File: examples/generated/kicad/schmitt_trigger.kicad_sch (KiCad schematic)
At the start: 6 parts

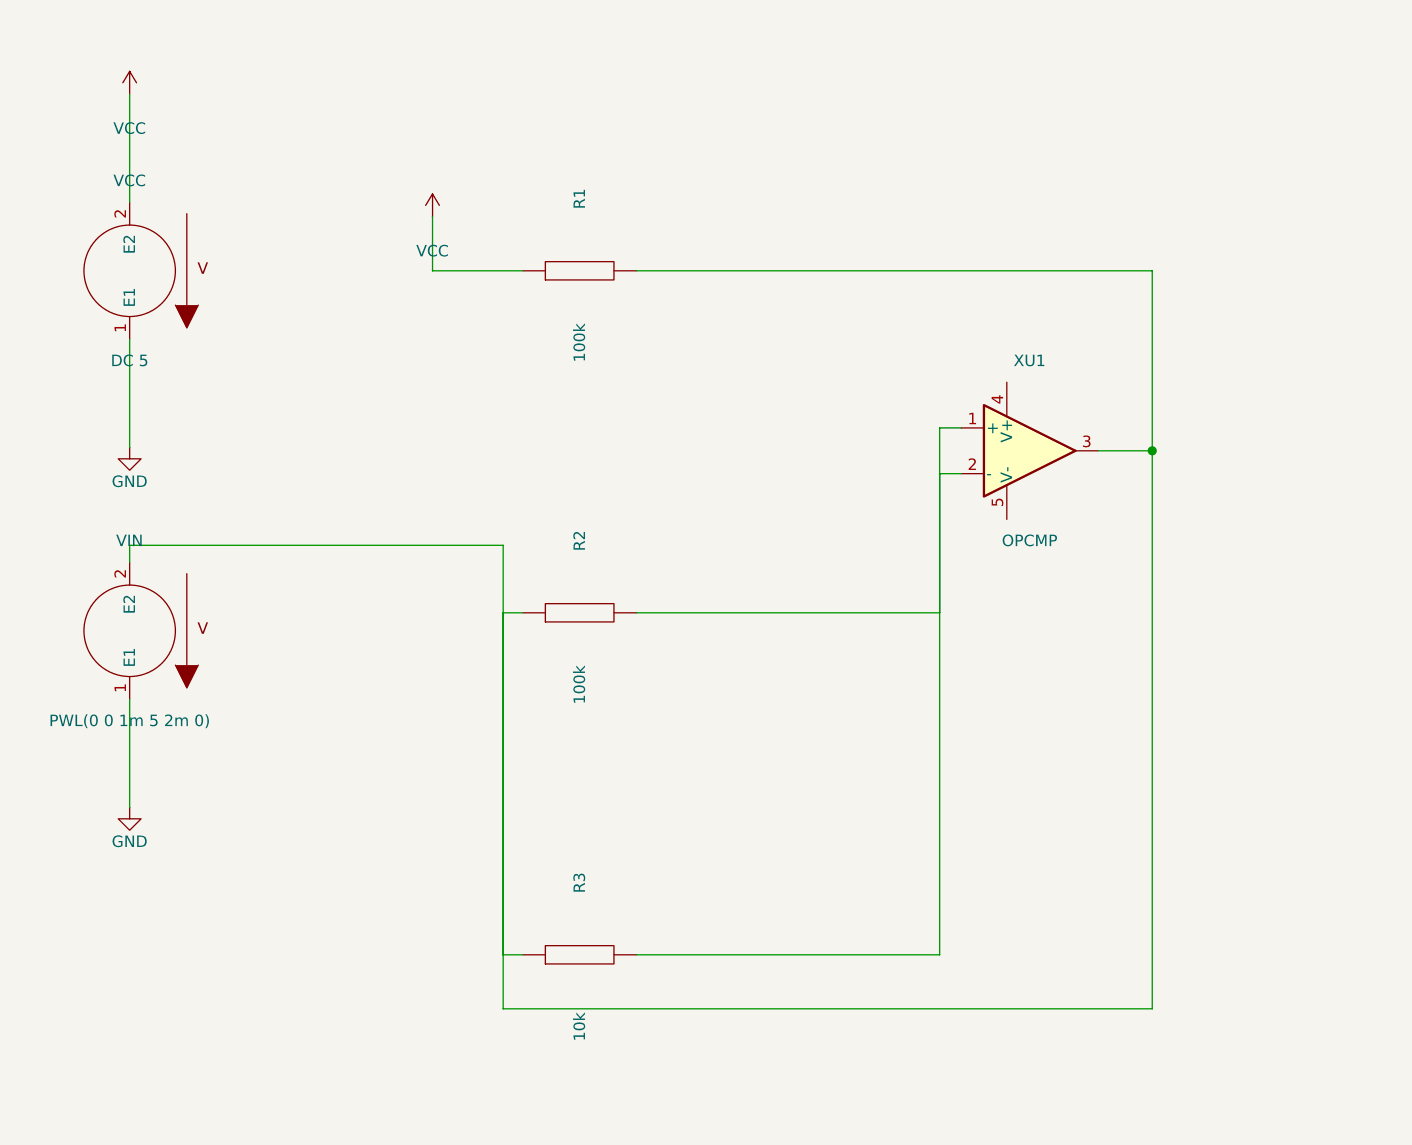
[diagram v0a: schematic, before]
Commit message: Ensure connectivity matches, as measured by opamp connectivity.
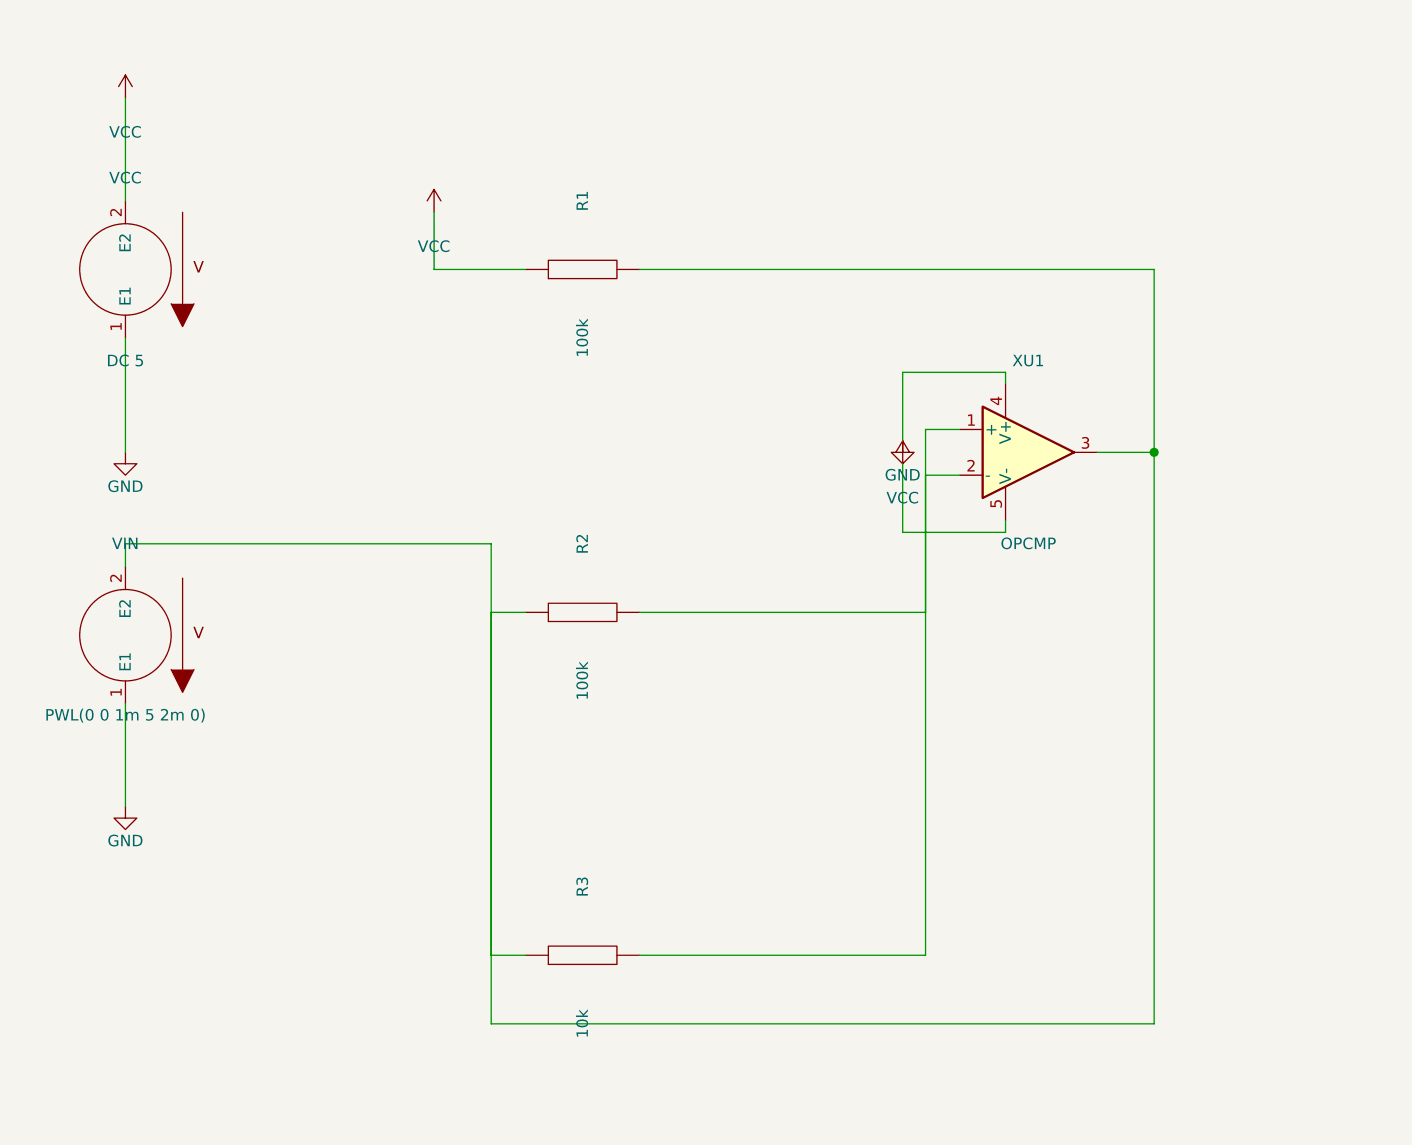
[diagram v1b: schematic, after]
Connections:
- net GND: now also XU1.4 (V+)
- net VCC: now also XU1.5 (V-)
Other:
- moved on the sheet: VIN

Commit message: Refactor further.
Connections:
- net GND: now also XU1.5 (V-); no longer XU1.4 (V+)
- net VCC: now also XU1.4 (V+); no longer XU1.5 (V-)
- net vout: now reaches R1.2, R2.1, R3.1, VIN.2 (E2), XU1.3
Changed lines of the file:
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@@
     )
   )
-  (symbol (lib_id "VCC") (at 135.89 91.44 0) (unit 1)
+  (symbol (lib_id "VCC") (at 147.32 69.85 0) (unit 1)
     (in_bom yes) (on_board yes)
-    (property "Reference" "#PWR0005" (at 135.89 87.63 0)
+    (property "Reference" "#PWR0005" (at 147.32 66.03999999999999 0)
       (effects (font (size 1.27 1.27)) hide)
     )
-    (property "Value" "VCC" (at 135.89 95.25 0)
+    (property "Value" "VCC" (at 147.32 73.66 0)
       (effects (font (size 1.27 1.27)))
     )
@@
     )
   )
-  (symbol (lib_id "GND") (at 135.89 88.90 0) (unit 1)
+  (symbol (lib_id "GND") (at 147.32 109.22 0) (unit 1)
     (in_bom yes) (on_board yes)
-    (property "Reference" "#PWR0006" (at 135.89 85.09 0)
+    (property "Reference" "#PWR0006" (at 147.32 105.41 0)
       (effects (font (size 1.27 1.27)) hide)
     )
-    (property "Value" "GND" (at 135.89 92.71000000000001 0)
+    (property "Value" "GND" (at 147.32 113.03 0)
       (effects (font (size 1.27 1.27)))
     )
@@
       (effects (font (size 1.27 1.27)) hide)
     )
+  )
+  (label "vin" (at 72.39 124.46 0)
+    (effects (font (size 1.27 1.27)))
+  )
+  (label "vminus" (at 124.46 119.38 0)
+    (effects (font (size 1.27 1.27)))
+  )
+  (label "vout" (at 163.83 90.17 0)
+    (effects (font (size 1.27 1.27)))
+  )
+  (label "vplus" (at 124.46 97.79 0)
+    (effects (font (size 1.27 1.27)))
   )
   (wire (pts (xy 49.53 62.23) (xy 49.53 50.80))
@@
     (stroke (width 0) (type solid) (color 0 0 0 0))
   )
-  (wire (pts (xy 147.32 97.79) (xy 147.32 99.06))
+  (wire (pts (xy 147.32 82.55) (xy 147.32 69.85))
     (stroke (width 0) (type solid) (color 0 0 0 0))
   )
-  (wire (pts (xy 147.32 99.06) (xy 135.89 99.06))
-    (stroke (width 0) (type solid) (color 0 0 0 0))
-  )
-  (wire (pts (xy 135.89 99.06) (xy 135.89 91.44))
-    (stroke (width 0) (type solid) (color 0 0 0 0))
-  )
-  (wire (pts (xy 147.32 82.55) (xy 147.32 81.28))
-    (stroke (width 0) (type solid) (color 0 0 0 0))
-  )
-  (wire (pts (xy 147.32 81.28) (xy 135.89 81.28))
-    (stroke (width 0) (type solid) (color 0 0 0 0))
-  )
-  (wire (pts (xy 135.89 81.28) (xy 135.89 88.90))
+  (wire (pts (xy 147.32 97.79) (xy 147.32 109.22))
     (stroke (width 0) (type solid) (color 0 0 0 0))
   )
@@
     (stroke (width 0) (type solid) (color 0 0 0 0))
   )
-  (wire (pts (xy 138.43 146.05) (xy 138.43 87.63))
+  (wire (pts (xy 138.43 146.05) (xy 138.43 92.71))
     (stroke (width 0) (type solid) (color 0 0 0 0))
   )
-  (wire (pts (xy 138.43 87.63) (xy 142.24 87.63))
+  (wire (pts (xy 138.43 92.71) (xy 142.24 92.71))
     (stroke (width 0) (type solid) (color 0 0 0 0))
   )
-  (wire (pts (xy 106.68 69.85) (xy 163.83 69.85))
+  (wire (pts (xy 106.68 69.85) (xy 110.49 69.85))
     (stroke (width 0) (type solid) (color 0 0 0 0))
   )
-  (wire (pts (xy 163.83 69.85) (xy 163.83 90.17))
+  (wire (pts (xy 110.49 69.85) (xy 110.49 44.45))
+    (stroke (width 0) (type solid) (color 0 0 0 0))
+  )
+  (wire (pts (xy 110.49 44.45) (xy 163.83 44.45))
+    (stroke (width 0) (type solid) (color 0 0 0 0))
+  )
+  (wire (pts (xy 163.83 44.45) (xy 163.83 90.17))
     (stroke (width 0) (type solid) (color 0 0 0 0))
   )
@@
     (stroke (width 0) (type solid) (color 0 0 0 0))
   )
-  (wire (pts (xy 138.43 107.95) (xy 138.43 92.71))
+  (wire (pts (xy 138.43 107.95) (xy 138.43 87.63))
     (stroke (width 0) (type solid) (color 0 0 0 0))
   )
-  (wire (pts (xy 138.43 92.71) (xy 142.24 92.71))
+  (wire (pts (xy 138.43 87.63) (xy 142.24 87.63))
     (stroke (width 0) (type solid) (color 0 0 0 0))
   )

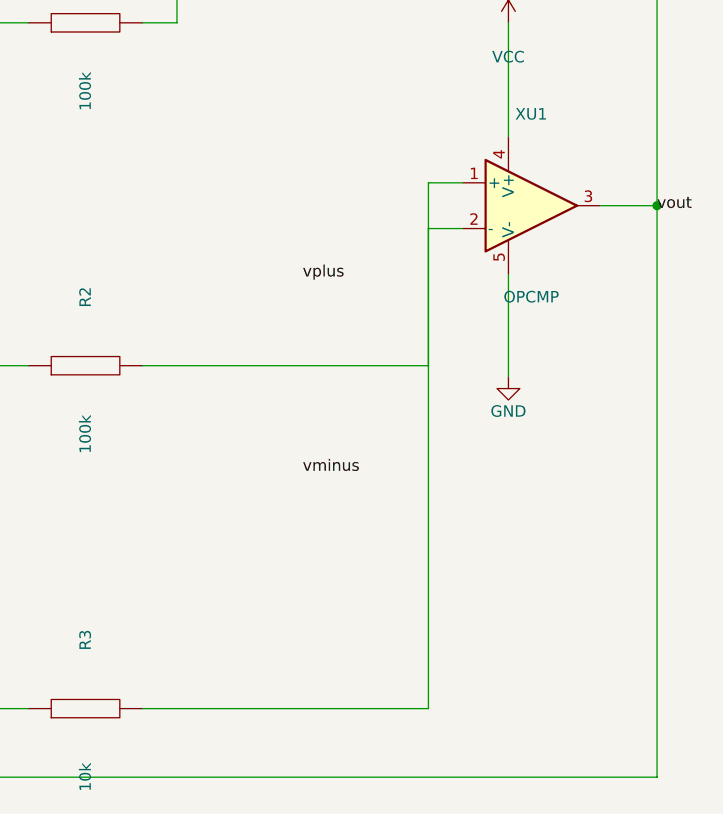
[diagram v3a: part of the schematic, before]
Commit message: Attempt to fix inverting op-amp circuit and related issues.
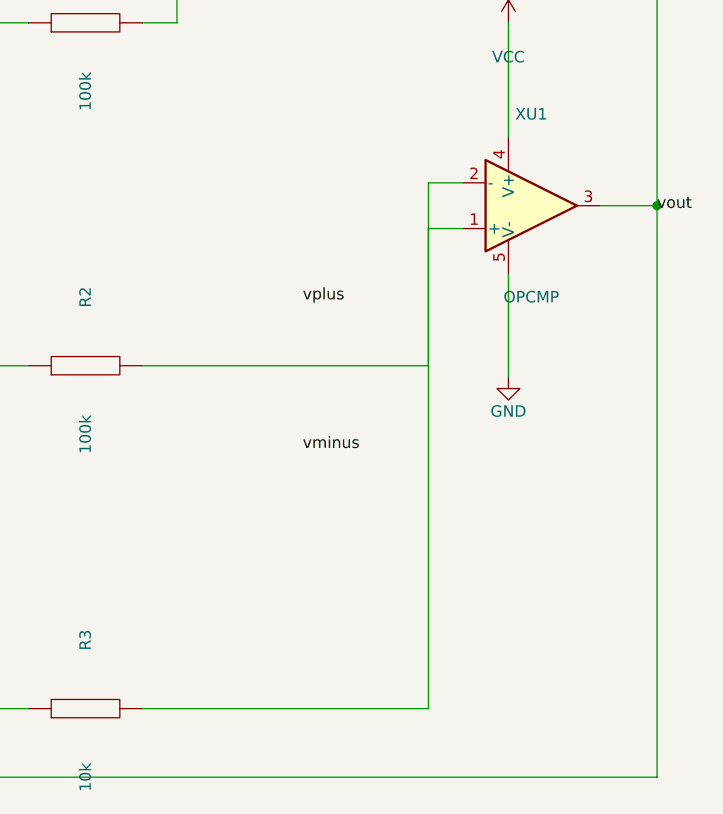
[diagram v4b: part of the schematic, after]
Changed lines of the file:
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@@
     (effects (font (size 1.27 1.27)))
   )
-  (label "vminus" (at 124.46 119.38 0)
+  (label "vminus" (at 124.46 116.84 0)
     (effects (font (size 1.27 1.27)))
   )
@@
     (effects (font (size 1.27 1.27)))
   )
-  (label "vplus" (at 124.46 97.79 0)
+  (label "vplus" (at 124.46 100.33 0)
     (effects (font (size 1.27 1.27)))
   )
@@
     (stroke (width 0) (type solid) (color 0 0 0 0))
   )
-  (wire (pts (xy 138.43 146.05) (xy 138.43 92.71))
+  (wire (pts (xy 138.43 146.05) (xy 138.43 87.63))
     (stroke (width 0) (type solid) (color 0 0 0 0))
   )
-  (wire (pts (xy 138.43 92.71) (xy 142.24 92.71))
+  (wire (pts (xy 138.43 87.63) (xy 142.24 87.63))
     (stroke (width 0) (type solid) (color 0 0 0 0))
   )
@@
     (stroke (width 0) (type solid) (color 0 0 0 0))
   )
-  (wire (pts (xy 138.43 107.95) (xy 138.43 87.63))
+  (wire (pts (xy 138.43 107.95) (xy 138.43 92.71))
     (stroke (width 0) (type solid) (color 0 0 0 0))
   )
-  (wire (pts (xy 138.43 87.63) (xy 142.24 87.63))
+  (wire (pts (xy 138.43 92.71) (xy 142.24 92.71))
     (stroke (width 0) (type solid) (color 0 0 0 0))
   )

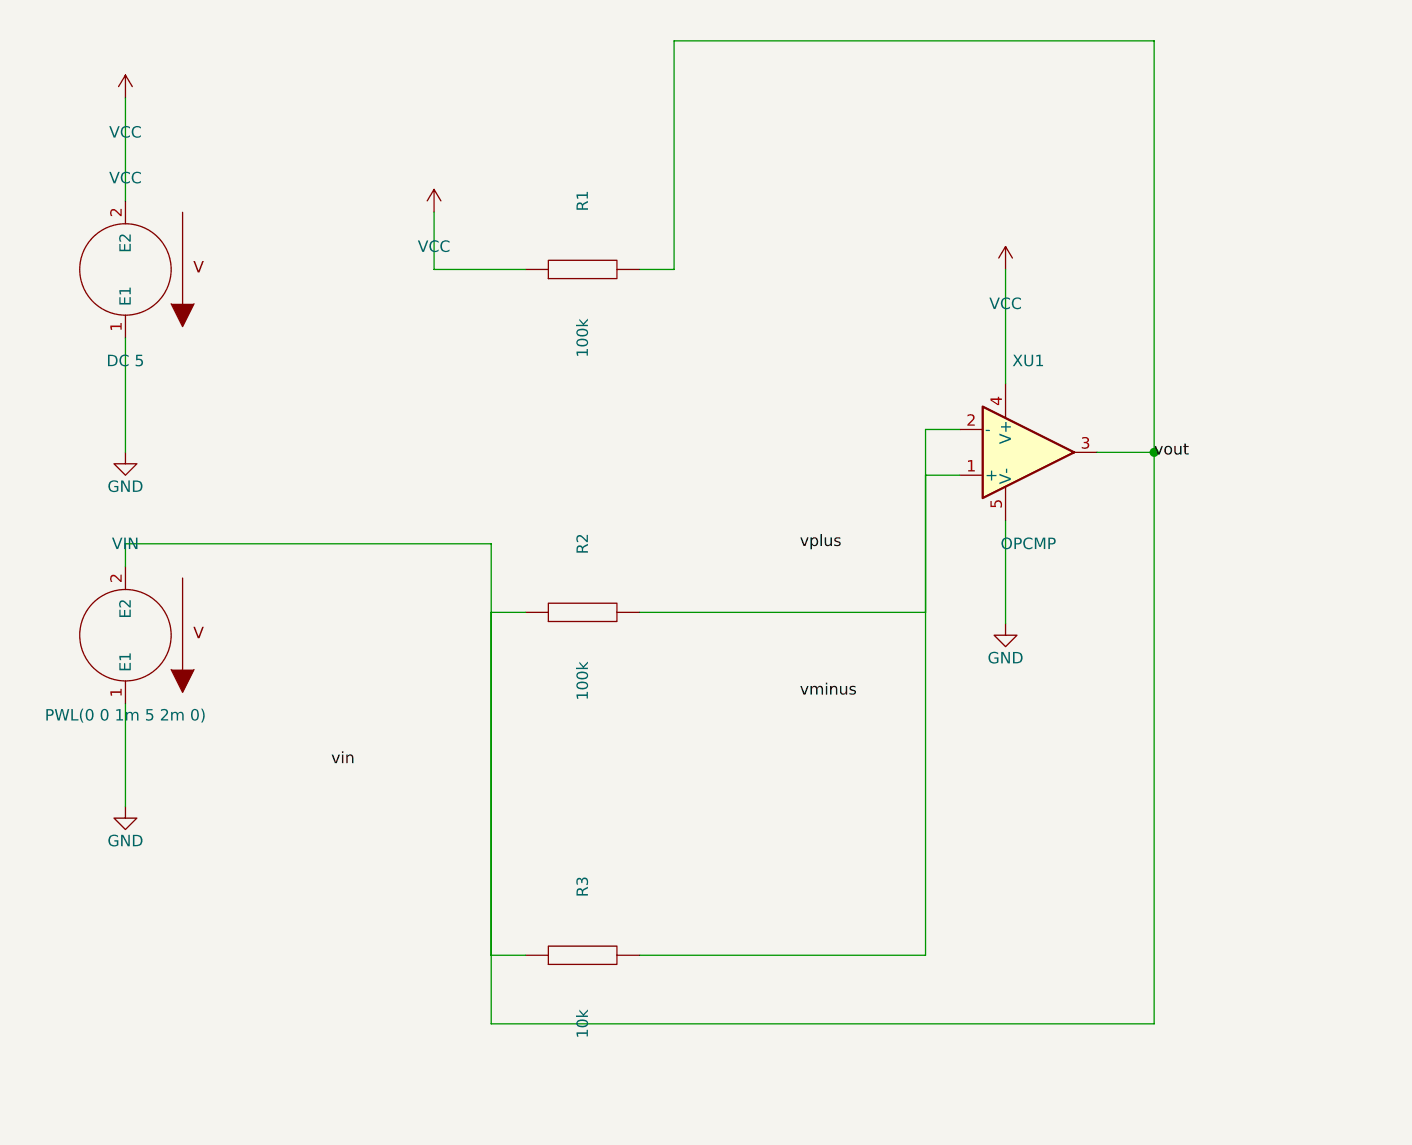
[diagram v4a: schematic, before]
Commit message: Attempt to add the right connections for the schmitt trigger. Messed up cmos inverter.
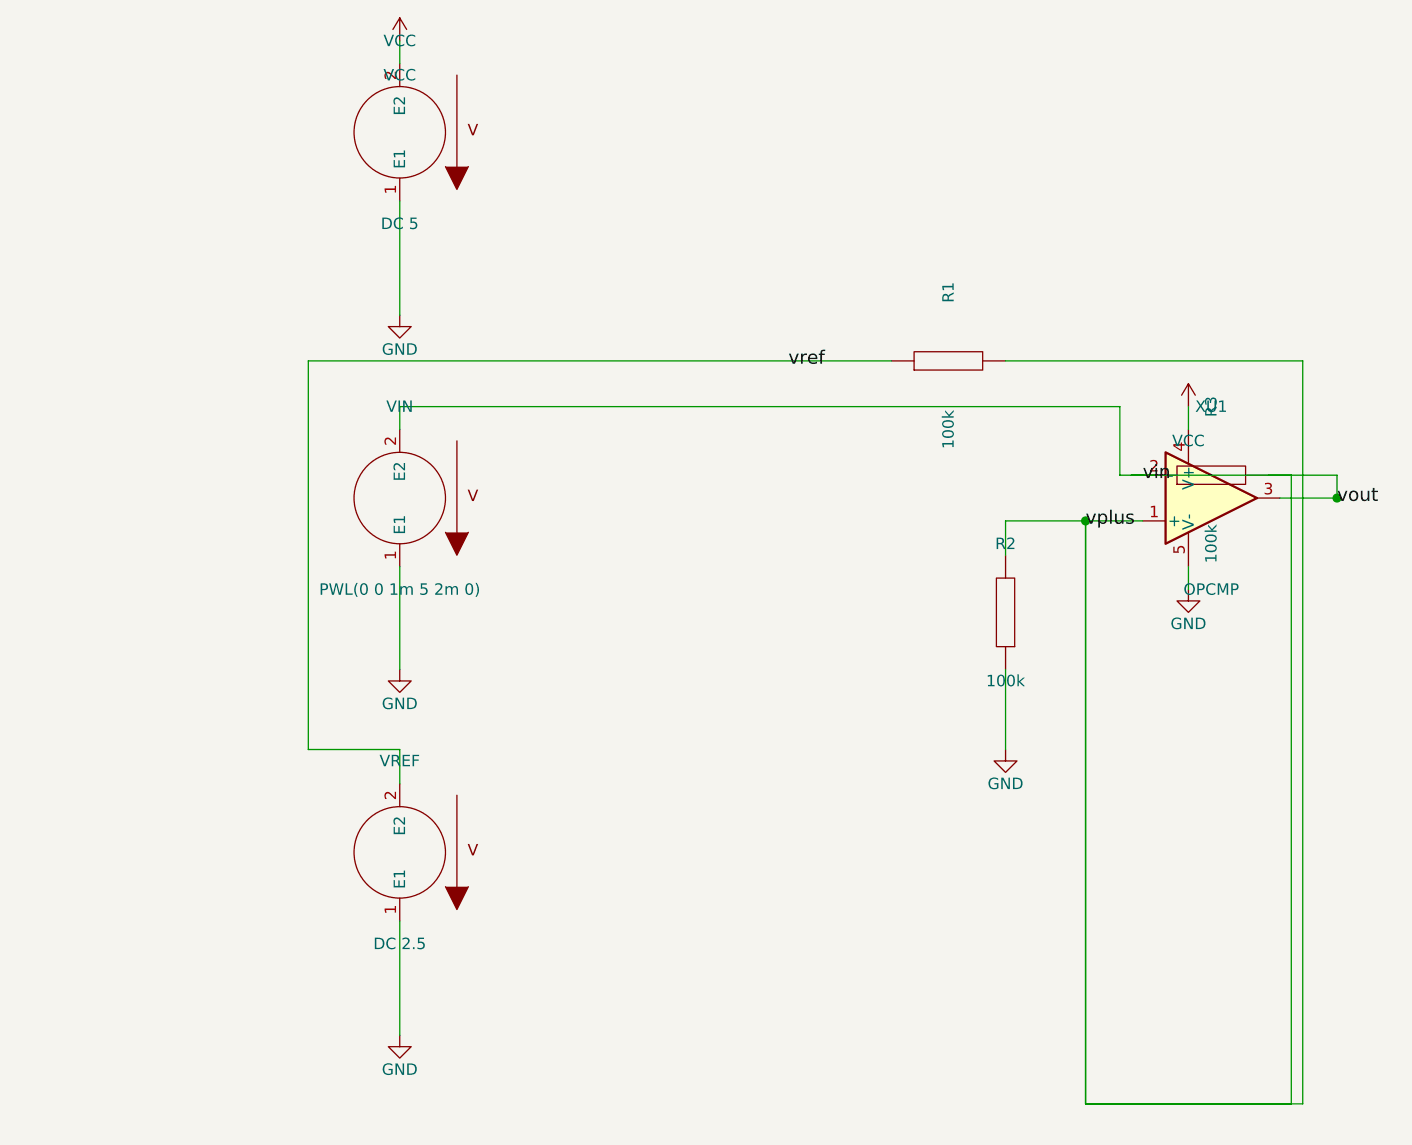
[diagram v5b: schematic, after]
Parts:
- added VREF: DC 2.5, symbol VSOURCE
- R3: value 10k -> 100k
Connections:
- net GND: now also R2.1, VREF.1 (E1)
- net VCC: no longer R1.1
- net vin: now also R1.2, R2.2, R3.1, R3.2, VIN.2 (E2), XU1.1 (+), XU1.2 (-), XU1.3
- removed net vout: R1.2, R2.1, R3.1, VIN.2 (E2), XU1.3
- new net vref: R1.1, VREF.2 (E2)
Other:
- moved on the sheet: R1, R2, R3, VCC, VIN, XU1
